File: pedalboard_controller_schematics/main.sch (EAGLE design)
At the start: 35 parts, among them IC1 74LS139N, IC2 74LS148N, IC3 7805TV, IC4 74LS279N, K1 TQ2-L-5V, K2 TQ2-L-5V, K3 TQ2-L-5V, K4 TQ2-L-5V, SW1 MOMENTARY-SWITCH-SPSTGENERIC, SW2 MOMENTARY-SWITCH-SPSTGENERIC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

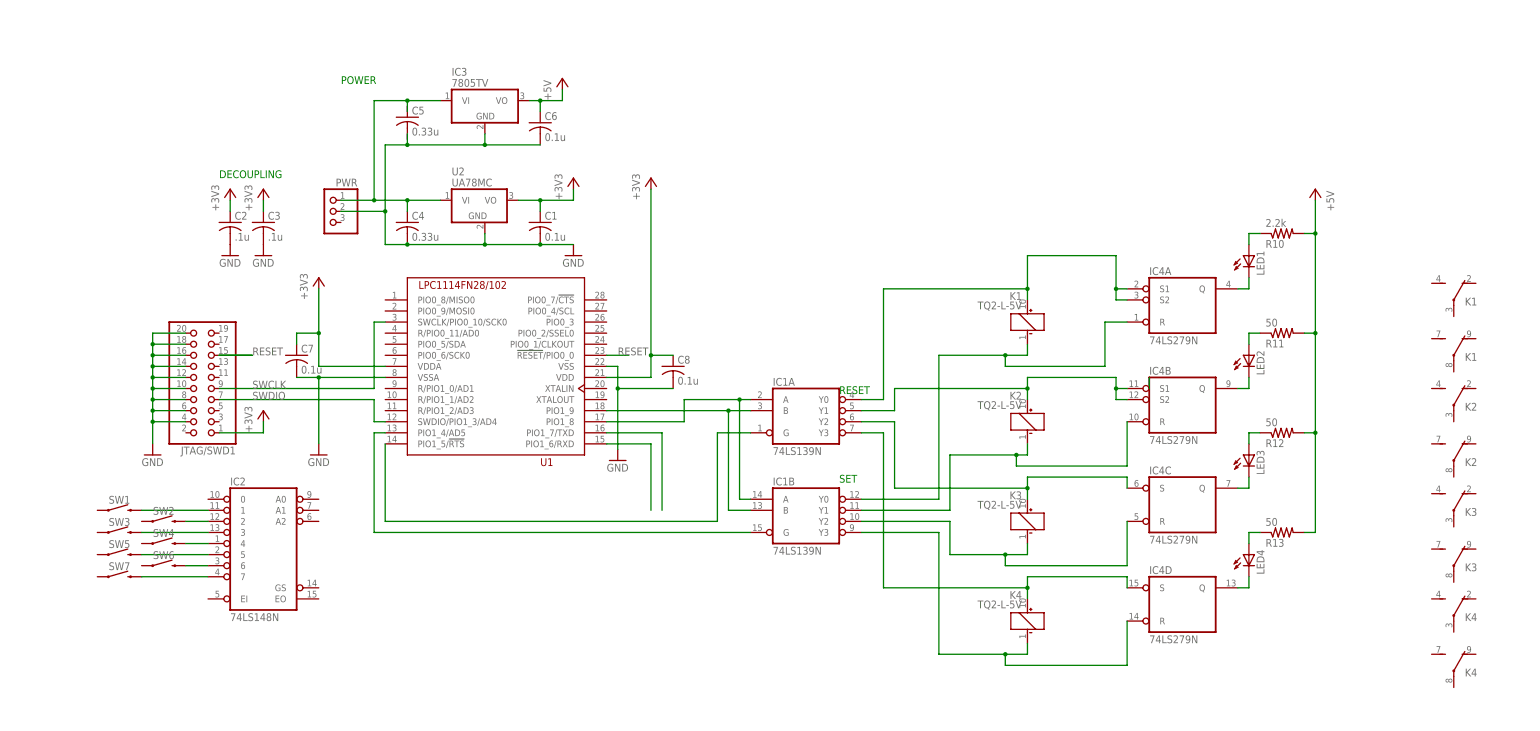
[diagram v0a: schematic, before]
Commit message: Added parts to EAGLE libraries, added switching section in schematic
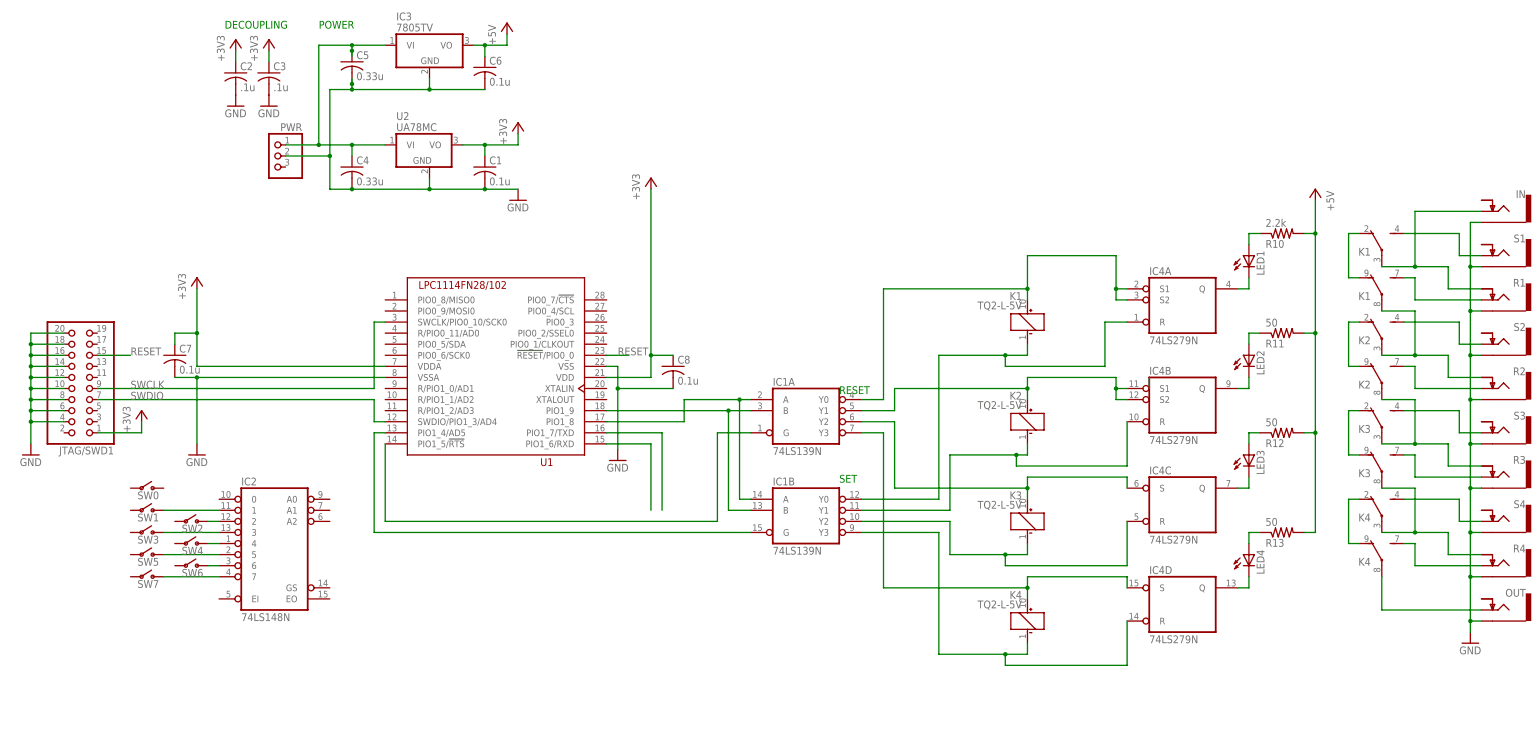
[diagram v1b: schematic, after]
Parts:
- added IN, OUT, R1, R2, R3, R4, S1, S2, S3, S4: AUDIO-JACK-NORM-TS, SparkFun-Connectors:AUDIO-JACK-NORM-TS
- added SW0: SWITCH-SPST, SparkFun-Switches:SWITCH-SPST
- SW1, SW2, SW3, SW4, SW5, SW6, SW7: value MOMENTARY-SWITCH-SPSTGENERIC -> SWITCH-SPST; device SparkFun-Switches:MOMENTARY-SWITCH-SPSTGENERIC -> SparkFun-Switches:SWITCH-SPST
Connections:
- new net N$32: IN.T, K11.P, R1.TS
- new net N$33: K11.O, K12.O
- new net N$34: K12.S, R1.T
- new net N$35: K11.S, S1.T
- new net N$36: K12.P, K21.P, R2.TS
- new net N$37: K21.O, K22.O
- new net N$38: K21.S, S2.T
- new net N$39: K22.S, R2.T
- new net N$40: K22.P, K31.P, R3.TS
- new net N$41: K31.S, S3.T
- new net N$42: K31.O, K32.O
- new net N$43: K32.S, R3.T
- new net N$45: K32.P, K41.P, R4.TS
- new net N$46: K41.O, K42.O
- new net N$47: K41.S, S4.T
- new net N$48: K42.S, R4.T
- new net N$50: K42.P, OUT.T
- net GND: now also C5.2, IN.S, OUT.S, R1.S, R2.S, R3.S, R4.S, S1.S, S2.S, S3.S, S4.S
- net N$2: now also C5.1
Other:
- moved on the sheet: C1, C2, C3, C4, C5, C6, C7, IC2, IC3, JTAG/SWD1, K1, K2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

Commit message: fixed encoder section
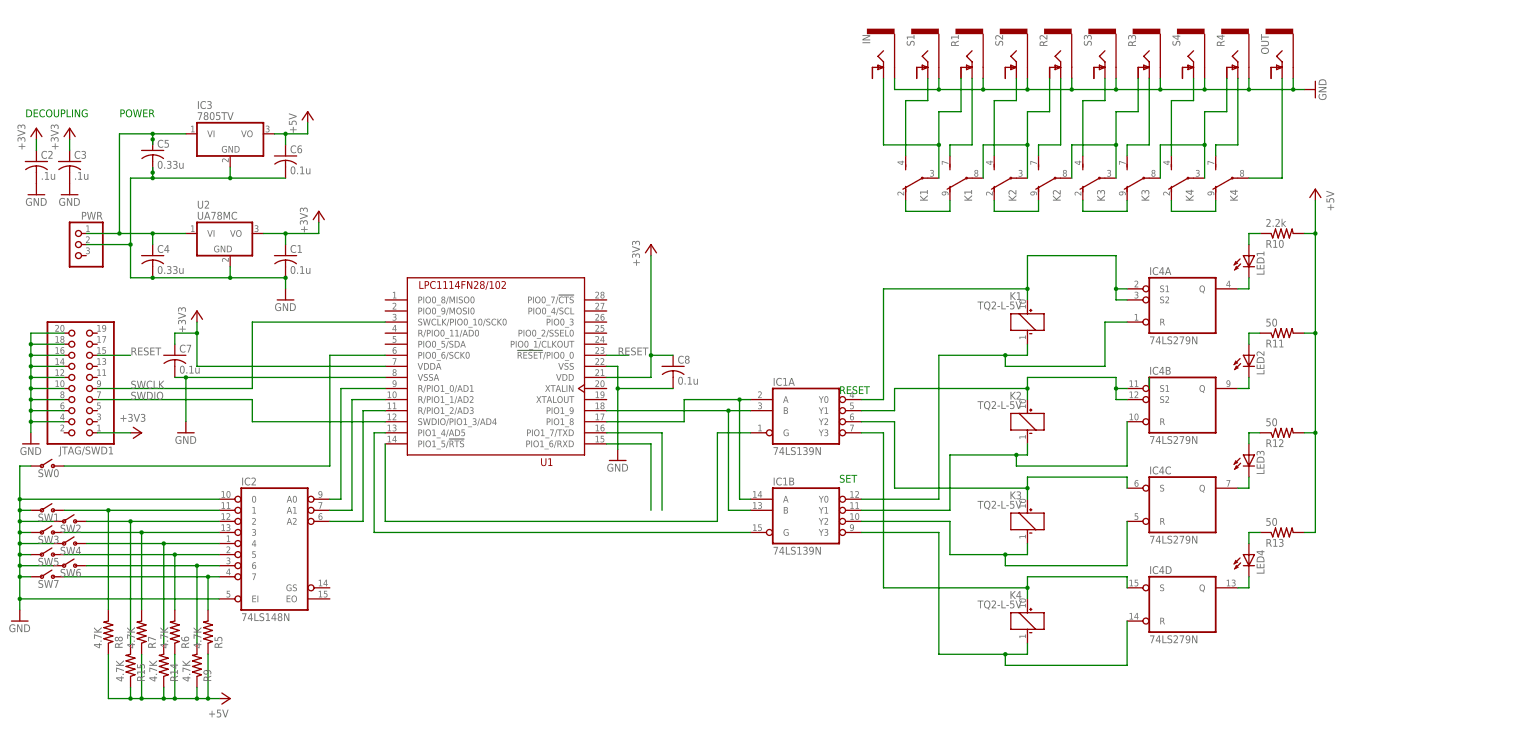
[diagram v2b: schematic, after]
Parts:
- added R14, R15, R5, R6, R7, R8, R9: 4.7K, resistor:R-US_0204/7
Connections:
- new net N$44: IC2A.A0, U1.R/PIO1_0/AD1
- new net N$49: IC2A.A1, U1.R/PIO1_1/AD2
- new net N$51: IC2A.A2, U1.R/PIO1_2/AD3
- new net N$52: SW0.2, U1.PIO0_6/SCK0
- net +5V: now also R14.1, R15.1, R5.1, R6.1, R7.1, R8.1, R9.1
- net GND: now also IC2A.0, IC2A.EI, SW0.3, SW1.3, SW2.3, SW3.3, SW4.3, SW5.3, SW6.3, SW7.3
- net N$26: now also R15.2
- net N$27: now also R7.2
- net N$28: now also R14.2
- net N$29: now also R6.2
- net N$30: now also R9.2
- net N$31: now also R5.2
- net N$4: now also R8.2
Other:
- moved on the sheet: C1, C2, C3, C4, C5, C6, IC3, IN, K1, K2, K3, K4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

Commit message: updated main board
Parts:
- removed PWR: (no value), pinhead:PINHD-1X3
- added J1: POWER_JACKPTH, SparkFun-Connectors:POWER_JACKPTH
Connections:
- net GND: now also J1.PWR; no longer PWR.2
- net N$2: now also J1.GND; no longer PWR.1
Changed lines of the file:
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@@
 <part name="IC2" library="74xx-us" deviceset="74*148" device="N" technology="LS"/>
 <part name="U1" library="lpc_11xx" deviceset="LPC1114FN28/102" device=""/>
-<part name="PWR" library="pinhead" deviceset="PINHD-1X3" device=""/>
 <part name="U2" library="lpc_11xx" deviceset="UA78M*C" device=""/>
 <part name="C1" library="rcl" deviceset="C-US" device="050-024X044" value="0.1u"/>
@@
 <part name="R14" library="resistor" deviceset="R-US_" device="0204/7" value="4.7K"/>
 <part name="R15" library="resistor" deviceset="R-US_" device="0204/7" value="4.7K"/>
+<part name="J1" library="SparkFun-Connectors" deviceset="POWER_JACK" device="PTH"/>
 </parts>
 <sheets>
@@
 <instance part="IC2" gate="A" x="25.4" y="-17.78"/>
 <instance part="U1" gate="G$1" x="76.2" y="20.32"/>
-<instance part="PWR" gate="A" x="-20.32" y="50.8" rot="MR0"/>
 <instance part="U2" gate="G$1" x="15.24" y="50.8"/>
 <instance part="C1" gate="G$1" x="27.94" y="48.26"/>
@@
 <instance part="R14" gate="G$1" x="0" y="-45.72" rot="MR90"/>
 <instance part="R15" gate="G$1" x="-7.62" y="-45.72" rot="MR90"/>
+<instance part="J1" gate="G$1" x="-22.86" y="55.88" rot="MR180"/>
 </instances>
 <busses>
@@
 <segment>
 <pinref part="U2" gate="G$1" pin="VI"/>
-<pinref part="PWR" gate="A" pin="1"/>
 <pinref part="C4" gate="G$1" pin="1"/>
 <wire x1="5.08" y1="53.34" x2="-2.54" y2="53.34" width="0.1524" layer="91"/>
 <wire x1="-2.54" y1="53.34" x2="-10.16" y2="53.34" width="0.1524" layer="91"/>
-<wire x1="-10.16" y1="53.34" x2="-17.78" y2="53.34" width="0.1524" layer="91"/>
+<wire x1="-10.16" y1="53.34" x2="-20.32" y2="53.34" width="0.1524" layer="91"/>
 <wire x1="-2.54" y1="50.8" x2="-2.54" y2="53.34" width="0.1524" layer="91"/>
 <junction x="-2.54" y="53.34"/>
@@
 <wire x1="-2.54" y1="76.2" x2="-2.54" y2="74.93" width="0.1524" layer="91"/>
 <pinref part="IC3" gate="A1" pin="VI"/>
-<wire x1="-2.54" y1="74.93" x2="-2.54" y2="73.66" width="0.1524" layer="91"/>
 <wire x1="-2.54" y1="76.2" x2="5.08" y2="76.2" width="0.1524" layer="91"/>
 <junction x="-2.54" y="76.2"/>
 <pinref part="C5" gate="G$1" pin="1"/>
-<junction x="-2.54" y="74.93"/>
+<pinref part="J1" gate="G$1" pin="GND"/>
 </segment>
 </net>
@@
 <net name="GND" class="0">
 <segment>
-<wire x1="-17.78" y1="50.8" x2="-7.62" y2="50.8" width="0.1524" layer="91"/>
-<wire x1="-7.62" y1="50.8" x2="-7.62" y2="43.18" width="0.1524" layer="91"/>
+<wire x1="-20.32" y1="48.26" x2="-7.62" y2="48.26" width="0.1524" layer="91"/>
+<wire x1="-7.62" y1="48.26" x2="-7.62" y2="43.18" width="0.1524" layer="91"/>
 <wire x1="-7.62" y1="43.18" x2="-2.54" y2="43.18" width="0.1524" layer="91"/>
 <wire x1="-2.54" y1="43.18" x2="15.24" y2="43.18" width="0.1524" layer="91"/>
@@
 <junction x="27.94" y="43.18"/>
 <pinref part="U2" gate="G$1" pin="GND"/>
-<pinref part="PWR" gate="A" pin="2"/>
 <pinref part="C1" gate="G$1" pin="2"/>
 <pinref part="GND1" gate="1" pin="GND"/>
@@
 <wire x1="15.24" y1="66.04" x2="-2.54" y2="66.04" width="0.1524" layer="91"/>
 <wire x1="-2.54" y1="66.04" x2="-7.62" y2="66.04" width="0.1524" layer="91"/>
-<wire x1="-7.62" y1="66.04" x2="-7.62" y2="50.8" width="0.1524" layer="91"/>
-<junction x="-7.62" y="50.8"/>
-<wire x1="-2.54" y1="68.58" x2="-2.54" y2="67.31" width="0.1524" layer="91"/>
+<wire x1="-7.62" y1="66.04" x2="-7.62" y2="48.26" width="0.1524" layer="91"/>
+<junction x="-7.62" y="48.26"/>
 <junction x="-2.54" y="66.04"/>
 <pinref part="IC3" gate="A1" pin="GND"/>
@@
 <junction x="15.24" y="66.04"/>
 <pinref part="C5" gate="G$1" pin="2"/>
-<junction x="-2.54" y="67.31"/>
-</segment>
-<segment>
+<pinref part="J1" gate="G$1" pin="PWR"/>
+</segment>
+<segment>

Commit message: finalized PCB
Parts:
- removed R12, R13: 50, resistor:R-US_0204/7
- removed R14, R15: 4.7K, resistor:R-US_0204/7
- added I1, I2, I3, I4: AUDIO-JACK-NORM-TS, SparkFun-Connectors:AUDIO-JACK-NORM-TS
- added J2, J3: (no value), SparkFun-Connectors:M14
- R1, R2, R3, R4: value AUDIO-JACK-NORM-TS -> 4.7K; device SparkFun-Connectors:AUDIO-JACK-NORM-TS -> resistor:R-US_0204/7
- R10: value 2.2k -> 2.2K
- R11: value 50 -> 2.2K
- R8: value 4.7K -> 2.2k
- R9: value 4.7K -> 2.2K
- renumbered IN to I0, OUT to O5, S1 to O1, S2 to O2, S3 to O3, S4 to O4
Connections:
- new net N$53: J2.10, U1.PIO0_5/SDA
- new net N$54: J2.11, U1.R/PIO0_11/AD0
- new net N$55: J2.13, U1.PIO0_9/MOSI0
- new net N$56: J2.14, U1.PIO0_8/MISO0
- new net N$57: J3.1, U1.PIO0_7/!CTS
- new net N$58: J3.2, U1.PIO0_4/SCL
- new net N$59: J3.3, U1.PIO0_3
- new net N$60: J3.4, U1.PIO0_2/SSEL0
- new net N$61: J3.5, U1.PIO0_1/CLKOUT
- new net N$62: J3.9, U1.XTALIN
- new net N$63: J3.10, U1.XTALOUT
- net +3V3: now also J2.8, J3.8
- net +5V: now also IC1P.VCC, IC2P.VCC, IC4P.VCC, R1.1, R2.1, R3.1, R4.1, R8.2, R9.2; no longer R12.2, R13.2, R14.1, R15.1, R8.1, R9.1
- net GND: now also I1.S, I2.S, I3.S, I4.S, J2.7, J3.7; no longer R1.S, R2.S, R3.S, R4.S
- net N$1: now also J3.14
- net N$21: now also R8.1; no longer R10.1
- net N$22: now also R9.1; no longer R11.1
- net N$23: now also R10.1; no longer R12.1
- net N$24: now also R11.1; no longer R13.1
- net N$25: now also J3.12
- net N$26: now also R2.2; no longer R15.2
- net N$27: now also R3.2; no longer R7.2
- net N$28: now also R4.2; no longer R14.2
- net N$29: now also R5.2; no longer R6.2
- net N$3: now also J3.13
- net N$30: now also R6.2; no longer R9.2
- net N$31: now also R7.2; no longer R5.2
- net N$32: now also I1.TS; no longer R1.TS
- net N$34: now also I1.T; no longer R1.T
- net N$36: now also I2.TS; no longer R2.TS
- net N$39: now also I2.T; no longer R2.T
- net N$4: now also R1.2; no longer R8.2
- net N$40: now also I3.TS; no longer R3.TS
- net N$43: now also I3.T; no longer R3.T
- net N$44: now also J2.6
- net N$45: now also I4.TS; no longer R4.TS
- net N$48: now also I4.T; no longer R4.T
- net N$49: now also J2.5
- net N$5: now also J3.11
- net N$51: now also J2.4
- net N$52: now also J2.9
- net N$6: now also J2.2
- net N$7: now also J2.1
- net RESET: now also J3.6
- net SWCLK: now also J2.12
- net SWDIO: now also J2.3
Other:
- moved on the sheet: C8, IC2, R10, R11, R5, R6, R7, R8, R9
